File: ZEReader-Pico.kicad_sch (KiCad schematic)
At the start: 4 parts

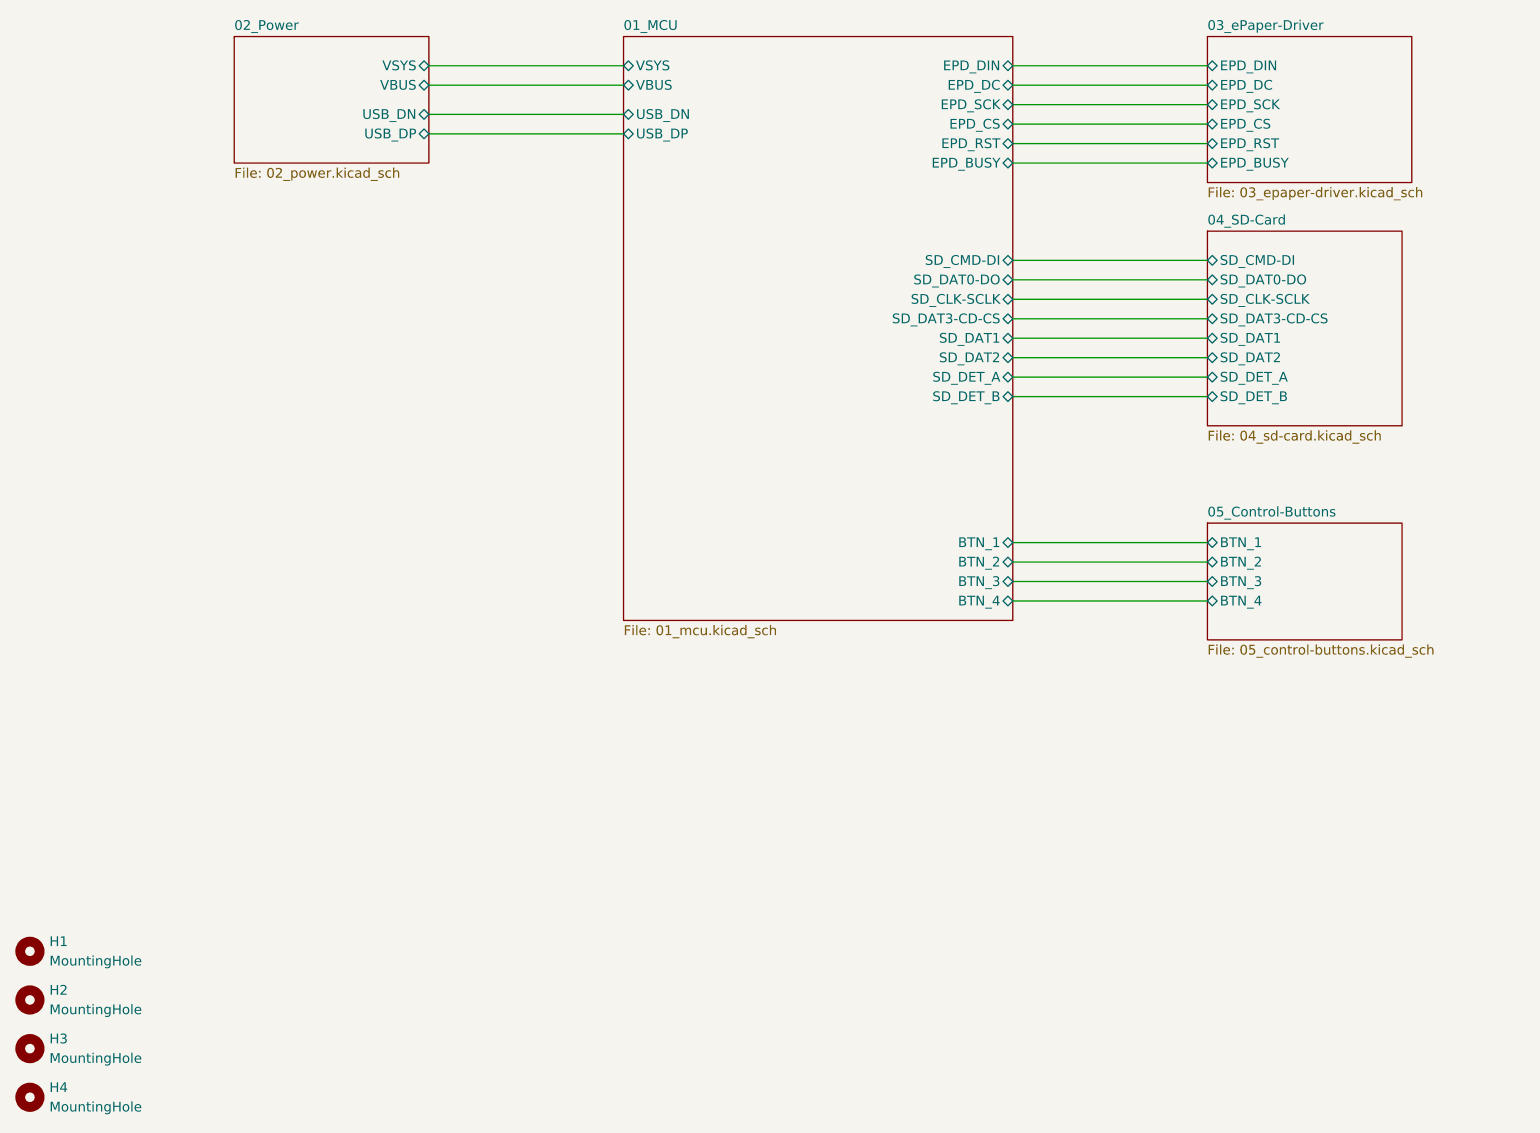
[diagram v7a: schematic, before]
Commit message: v2: major changes
- Move to hierarchical labels
- use another RP Pico Footprint
- split power path in USB/charging and on/off with a button approach in order to control turning on and off
  with the RP Pico, make use of long presses and delay turning of the voltage in order to do a proper shutdown
- introduce another charging controller with a better performance an a lower voltage needed in order to charge the battery
- rework display booster circuit
- rework SD and buttons
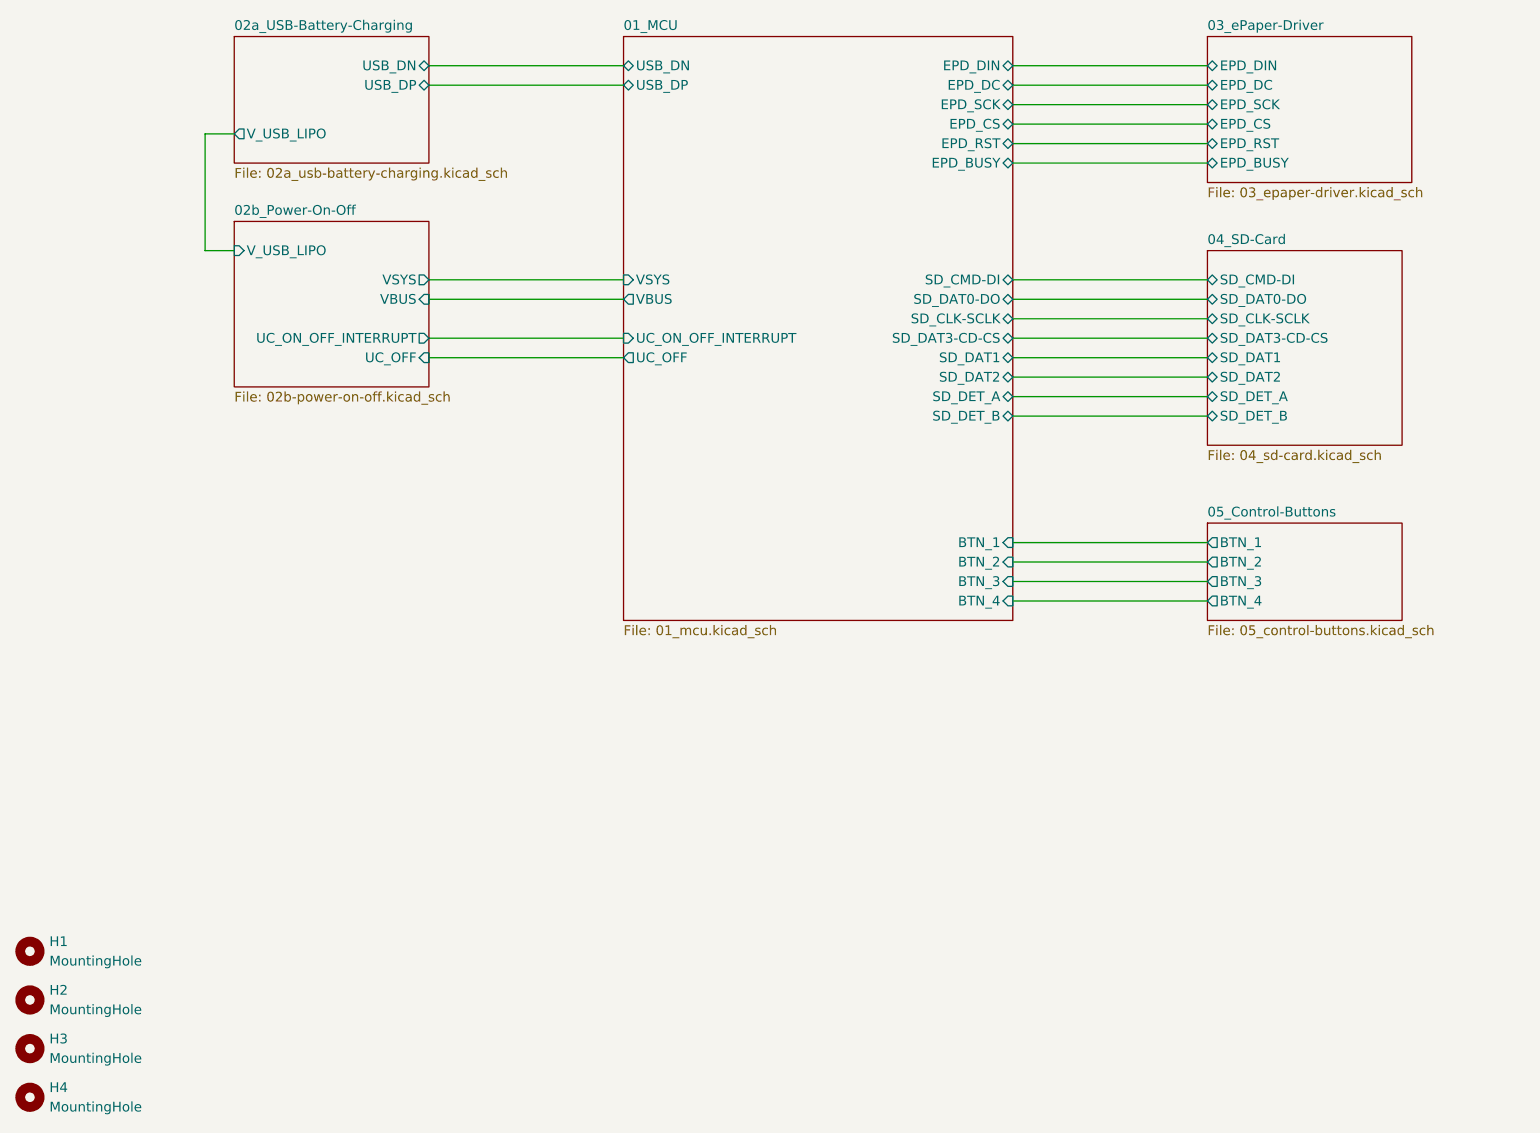
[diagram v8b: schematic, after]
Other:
- sheet 02_Power renamed 02a_USB-Battery-Charging
- added sheet 02b_Power-On-Off (02b-power-on-off.kicad_sch)
- sheet 01_MCU ports: added UC_OFF, UC_ON_OFF_INTERRUPT; removed none
- sheet 02a_USB-Battery-Charging: file 02_power.kicad_sch -> 02a_usb-battery-charging.kicad_sch
- sheet 02a_USB-Battery-Charging ports: added V_USB_LIPO; removed VBUS, VSYS
